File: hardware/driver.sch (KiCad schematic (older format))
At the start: 6 parts, among them J89 Conn_01x04, J90 Conn_01x04, J91 Conn_01x04, J92 Conn_01x04, J93 Conn_01x04

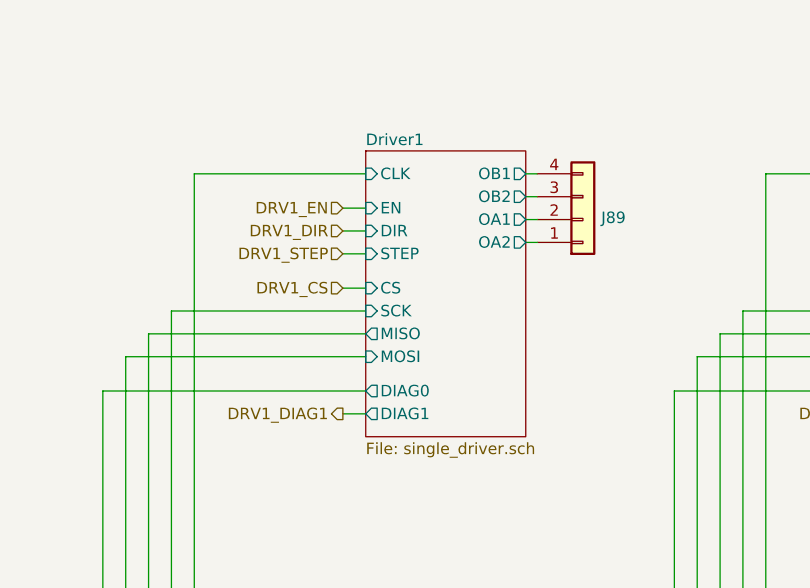
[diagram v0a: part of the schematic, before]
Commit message: replaced stepper driver
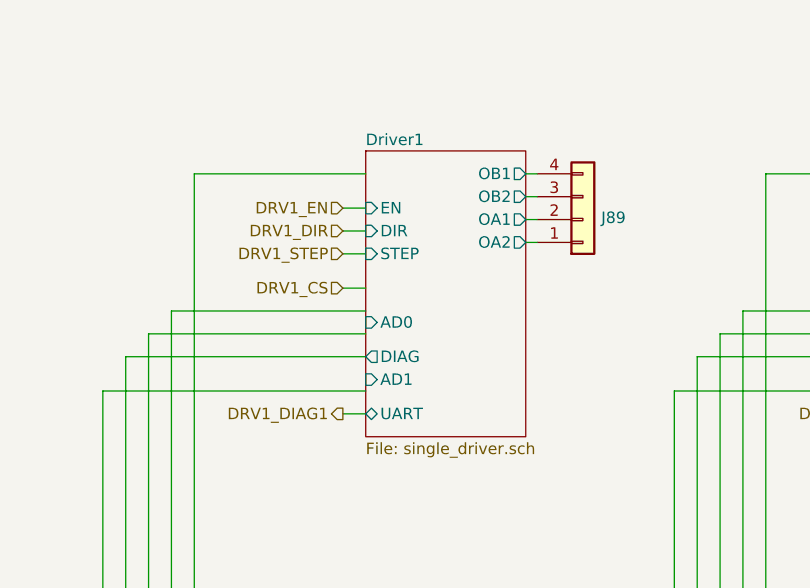
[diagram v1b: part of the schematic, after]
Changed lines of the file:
@@
 EESchema Schematic File Version 4
+LIBS:c3dpb-cache
 EELAYER 29 0
 EELAYER END
@@
 F0 "Driver1" 50
 F1 "single_driver.sch" 50
-F2 "CLK" I L 4150 2050 50
-F3 "CS" I L 4150 2550 50
-F4 "SCK" I L 4150 2650 50
-F5 "MISO" O L 4150 2750 50
-F6 "MOSI" I L 4150 2850 50
-F7 "STEP" I L 4150 2400 50
-F8 "DIR" I L 4150 2300 50
-F9 "EN" I L 4150 2200 50
-F10 "DIAG0" O L 4150 3000 50
-F11 "DIAG1" O L 4150 3100 50
-F12 "OA1" O R 4850 2250 50
-F13 "OA2" O R 4850 2350 50
-F14 "OB1" O R 4850 2050 50
-F15 "OB2" O R 4850 2150 50
+F2 "STEP" I L 4150 2400 50
+F3 "DIR" I L 4150 2300 50
+F4 "EN" I L 4150 2200 50
+F5 "OA1" O R 4850 2250 50
+F6 "OA2" O R 4850 2350 50
+F7 "OB1" O R 4850 2050 50
+F8 "OB2" O R 4850 2150 50
+F9 "AD0" I L 4150 2700 50
+F10 "AD1" I L 4150 2950 50
+F11 "UART" B L 4150 3100 50
+F12 "DIAG" O L 4150 2850 50
 $EndSheet
 Wire Wire Line
